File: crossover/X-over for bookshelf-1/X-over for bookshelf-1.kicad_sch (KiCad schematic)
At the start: 10 parts, among them J1 Screw_Terminal_01x02, J2 Screw_Terminal_01x04

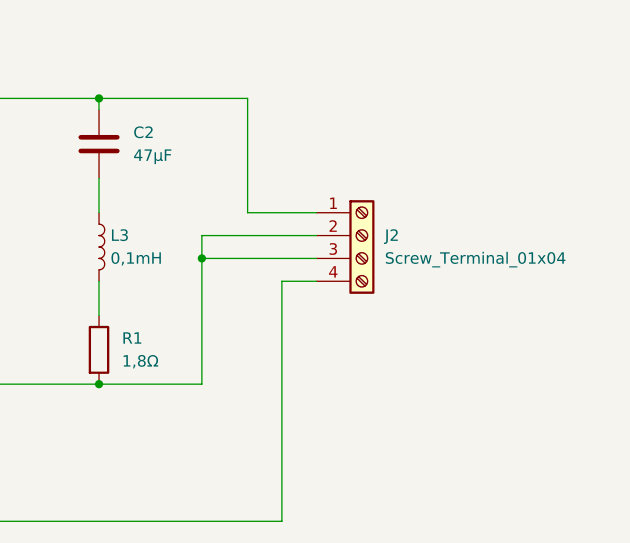
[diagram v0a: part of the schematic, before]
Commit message: Feature/pcb updates (#3)
* adding intial work to support PCB draw

* Minimizing overall PCB size

Now it should both fit inside the cabinet as well as through the driver opening.
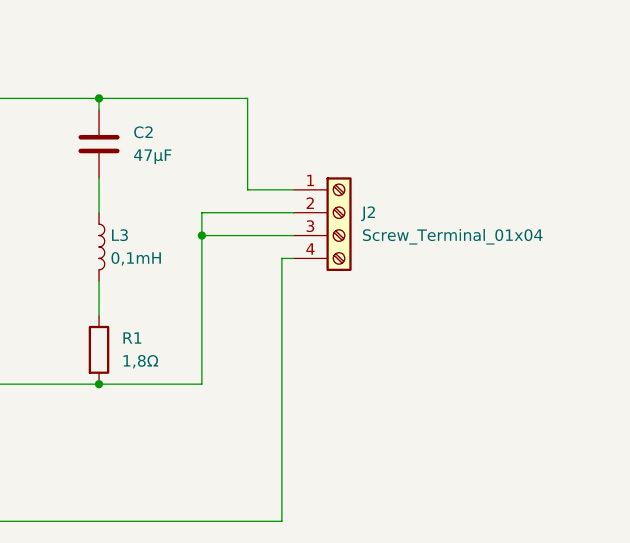
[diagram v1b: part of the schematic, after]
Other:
- moved on the sheet: J2
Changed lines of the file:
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@@
 (kicad_sch (version 20230121) (generator eeschema)
   (paper "A4")
-  (junction (at 176.53 111.76) (diameter 0) (color 0 0 0 0)
+  (junction (at 176.53 109.22) (diameter 0) (color 0 0 0 0)
   )
   (junction (at 115.57 140.97) (diameter 0) (color 0 0 0 0)
@@
   (junction (at 165.1 125.73) (diameter 0) (color 0 0 0 0)
   )
-  (wire (pts (xy 176.53 111.76) (xy 176.53 125.73))
-    (stroke (width 0) (type default))
-  )
   (wire (pts (xy 146.05 140.97) (xy 185.42 140.97))
     (stroke (width 0) (type default))
   )
+  (wire (pts (xy 176.53 109.22) (xy 176.53 106.68))
+    (stroke (width 0) (type default))
+  )
   (wire (pts (xy 165.1 93.98) (xy 181.61 93.98))
+    (stroke (width 0) (type default))
+  )
+  (wire (pts (xy 176.53 106.68) (xy 186.69 106.68))
     (stroke (width 0) (type default))
   )
@@
     (stroke (width 0) (type default))
   )
-  (wire (pts (xy 176.53 109.22) (xy 189.23 109.22))
-    (stroke (width 0) (type default))
-  )
   (wire (pts (xy 115.57 140.97) (xy 104.14 140.97))
     (stroke (width 0) (type default))
@@
     (stroke (width 0) (type default))
   )
-  (wire (pts (xy 181.61 106.68) (xy 189.23 106.68))
-    (stroke (width 0) (type default))
-  )
-  (wire (pts (xy 176.53 109.22) (xy 176.53 111.76))
+  (wire (pts (xy 181.61 104.14) (xy 186.69 104.14))
     (stroke (width 0) (type default))
   )
@@
     (stroke (width 0) (type default))
   )
-  (wire (pts (xy 185.42 140.97) (xy 185.42 114.3))
+  (wire (pts (xy 185.42 140.97) (xy 185.42 111.76))
     (stroke (width 0) (type default))
   )
@@
     (stroke (width 0) (type default))
   )
-  (wire (pts (xy 181.61 93.98) (xy 181.61 106.68))
+  (wire (pts (xy 181.61 93.98) (xy 181.61 104.14))
     (stroke (width 0) (type default))
   )
@@
     (stroke (width 0) (type default))
   )
-  (wire (pts (xy 185.42 114.3) (xy 189.23 114.3))
+  (wire (pts (xy 185.42 111.76) (xy 186.69 111.76))
     (stroke (width 0) (type default))
   )
-  (wire (pts (xy 176.53 111.76) (xy 189.23 111.76))
+  (wire (pts (xy 176.53 109.22) (xy 186.69 109.22))
     (stroke (width 0) (type default))
   )
@@
     (stroke (width 0) (type default))
   )
-  (symbol (lib_id "Connector:Screw_Terminal_01x04") (at 194.31 109.22 0) (unit 1)
+  (wire (pts (xy 176.53 109.22) (xy 176.53 125.73))
+    (stroke (width 0) (type default))
+  )
+  (symbol (lib_id "Connector:Screw_Terminal_01x04") (at 191.77 106.68 0) (unit 1)
     (in_bom yes) (on_board yes) (dnp no) (fields_autoplaced)
-    (property "Reference" "J2" (at 196.85 109.22 0)
+    (property "Reference" "J2" (at 194.31 106.68 0)
       (effects (font (size 1.27 1.27)) (justify left))
     )
-    (property "Value" "Screw_Terminal_01x04" (at 196.85 111.76 0)
+    (property "Value" "Screw_Terminal_01x04" (at 194.31 109.22 0)
       (effects (font (size 1.27 1.27)) (justify left))
     )
-    (property "Footprint" "Connector_Wire:SolderWire-0.5sqmm_1x04_P4.6mm_D0.9mm_OD2.1mm" (at 194.31 109.22 0)
+    (property "Footprint" "Connector_Wire:SolderWire-0.5sqmm_1x04_P4.6mm_D0.9mm_OD2.1mm" (at 191.77 106.68 0)
       (effects (font (size 1.27 1.27)) hide)
     )
-    (property "Datasheet" "~" (at 194.31 109.22 0)
+    (property "Datasheet" "~" (at 191.77 106.68 0)
       (effects (font (size 1.27 1.27)) hide)
     )

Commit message: adding holes
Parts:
- removed J1: Screw_Terminal_01x02, Connector_Wire:SolderWire-0.5sqmm_1x02_P4.6mm_D0.9mm_OD2.1mm, symbol Connector:Screw_Terminal_01x02
- removed J2: Screw_Terminal_01x04, Connector_Wire:SolderWire-0.5sqmm_1x04_P4.6mm_D0.9mm_OD2.1mm, symbol Connector:Screw_Terminal_01x04
- added J1: Conn_01x02_Pin, Connector_Wire:SolderWire-1sqmm_1x02_P7.8mm_D1.4mm_OD3.9mm, symbol Connector:Conn_01x02_Pin
- added J2: Conn_01x04_Pin, Connector_Wire:SolderWire-1sqmm_1x04_P7.8mm_D1.4mm_OD3.9mm, symbol Connector:Conn_01x04_Pin
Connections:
- net at C2.1, C3.2: now also J2.4 (Pin_4)
- net at C1.1, L2.2, R1.2: now also J2.2 (Pin_2), J2.3 (Pin_3)
- net at L1.2: now also J2.1 (Pin_1)
- net at C1.2, L1.1: now also J1.2 (Pin_2)
- net at L2.1, R2.1: now also J1.1 (Pin_1)
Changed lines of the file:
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@@
     (stroke (width 0) (type default))
-  )
-  (symbol (lib_id "Connector:Screw_Terminal_01x04") (at 191.77 106.68 0) (unit 1)
-    (in_bom yes) (on_board yes) (dnp no) (fields_autoplaced)
-    (property "Reference" "J2" (at 194.31 106.68 0)
-      (effects (font (size 1.27 1.27)) (justify left))
-    )
-    (property "Value" "Screw_Terminal_01x04" (at 194.31 109.22 0)
-      (effects (font (size 1.27 1.27)) (justify left))
-    )
-    (property "Footprint" "Connector_Wire:SolderWire-0.5sqmm_1x04_P4.6mm_D0.9mm_OD2.1mm" (at 191.77 106.68 0)
-      (effects (font (size 1.27 1.27)) hide)
-    )
-    (property "Datasheet" "~" (at 191.77 106.68 0)
-      (effects (font (size 1.27 1.27)) hide)
-    )
-    (pin "1")
-    (pin "2")
-    (pin "3")
-    (pin "4")
-    (instances
-      (project "X-over for bookshelf-1"
-        (path "/fc1d4b14-33b9-4bb9-bf19-11bc51b6ca66"
-          (reference "J2") (unit 1)
-        )
-      )
-    )
   )
   (symbol (lib_id "Device:C") (at 115.57 127 0) (unit 1)
@@
     )
   )
-  (symbol (lib_id "Connector:Screw_Terminal_01x02") (at 80.01 118.11 180) (unit 1)
+  (symbol (lib_id "Connector:Conn_01x02_Pin") (at 80.01 115.57 0) (unit 1)
     (in_bom yes) (on_board yes) (dnp no) (fields_autoplaced)
-    (property "Reference" "J1" (at 80.01 109.22 0)
+    (property "Reference" "J1" (at 80.645 110.49 0)
       (effects (font (size 1.27 1.27)))
     )
-    (property "Value" "Screw_Terminal_01x02" (at 80.01 111.76 0)
+    (property "Value" "Conn_01x02_Pin" (at 80.645 113.03 0)
       (effects (font (size 1.27 1.27)))
     )
-    (property "Footprint" "Connector_Wire:SolderWire-0.5sqmm_1x02_P4.6mm_D0.9mm_OD2.1mm" (at 80.01 118.11 0)
+    (property "Footprint" "Connector_Wire:SolderWire-1sqmm_1x02_P7.8mm_D1.4mm_OD3.9mm" (at 80.01 115.57 0)
       (effects (font (size 1.27 1.27)) hide)
     )
-    (property "Datasheet" "~" (at 80.01 118.11 0)
+    (property "Datasheet" "~" (at 80.01 115.57 0)
       (effects (font (size 1.27 1.27)) hide)
     )
@@
         )
       )
+    )
+  )
+  (symbol (lib_id "Connector:Conn_01x04_Pin") (at 191.77 109.22 180) (unit 1)
+    (in_bom yes) (on_board yes) (dnp no)
+    (property "Reference" "J2" (at 186.69 100.33 0)
+      (effects (font (size 1.27 1.27)) (justify right))
+    )
+    (property "Value" "Conn_01x04_Pin" (at 182.88 97.79 0)
+      (effects (font (size 1.27 1.27)) (justify right))
+    )
+    (property "Footprint" "Connector_Wire:SolderWire-1sqmm_1x04_P7.8mm_D1.4mm_OD3.9mm" (at 191.77 109.22 0)
+      (effects (font (size 1.27 1.27)) hide)
+    )
+    (property "Datasheet" "~" (at 191.77 109.22 0)
+      (effects (font (size 1.27 1.27)) hide)
+    )
+    (pin "1")
+    (pin "2")
+    (pin "3")
+    (pin "4")
+    (instances
+      (project "X-over for bookshelf-1"
+        (path "/fc1d4b14-33b9-4bb9-bf19-11bc51b6ca66"
+          (reference "J2") (unit 1)
+        )
+      )
